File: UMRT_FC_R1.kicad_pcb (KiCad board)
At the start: 2 copper layers, 85 parts, among them J1 Conn_01x02, J10 Conn_01x04_Pin, J2 Conn_01x02_Pin, J3 Conn_01x02_Pin, J4 Conn_01x02_Pin, J5 Conn_01x02_Pin, J6 Conn_01x02_Pin, J7 Conn_01x04_Pin, J8 Conn_01x04_Pin, J9 Conn_01x04_Pin, U7 RP2040, U8 W25Q128JVS, Y1 Crystal_GND24

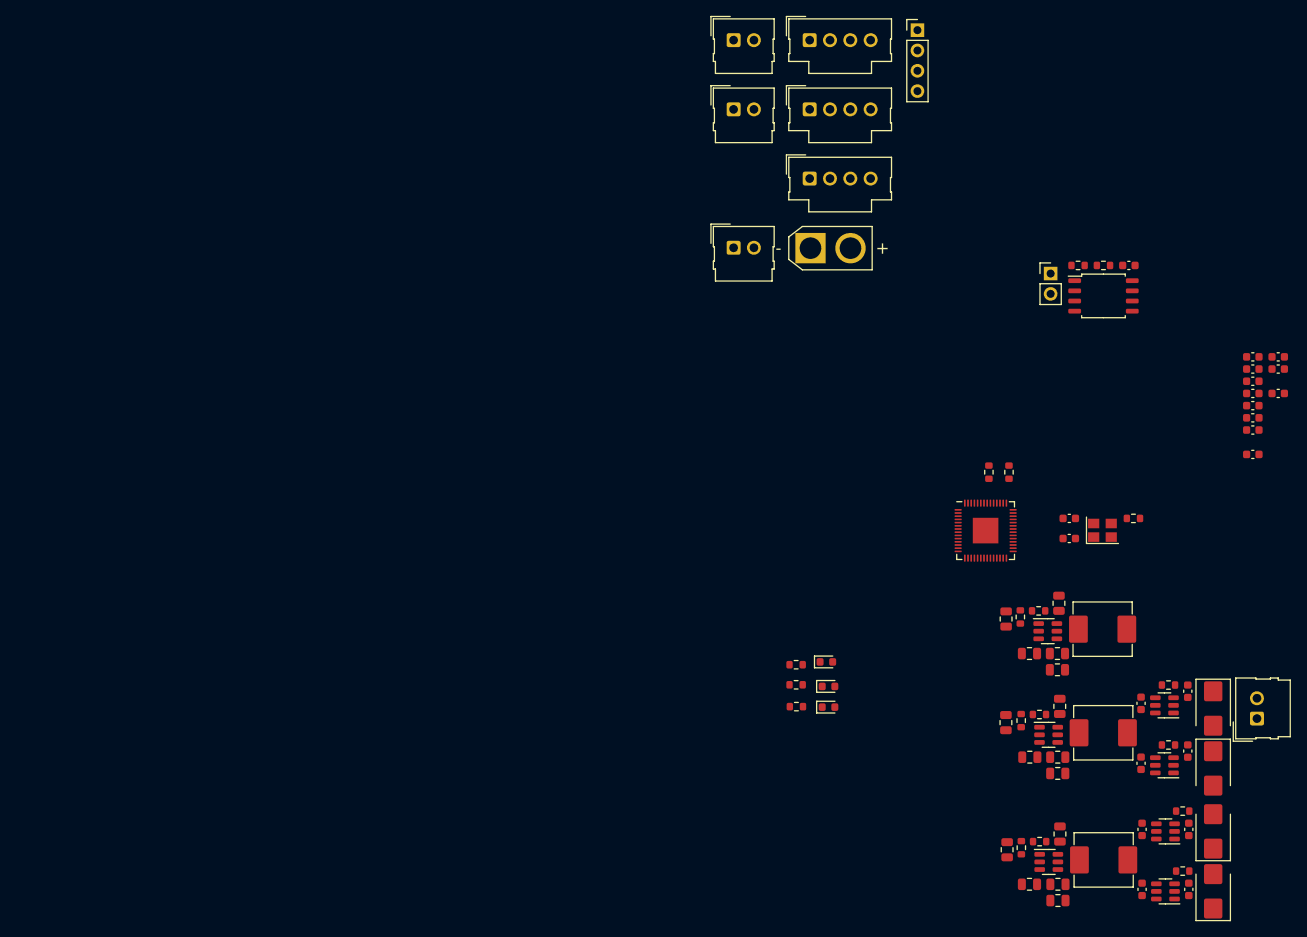
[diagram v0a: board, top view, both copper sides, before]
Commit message: started on layout and added SD/flash/BNO
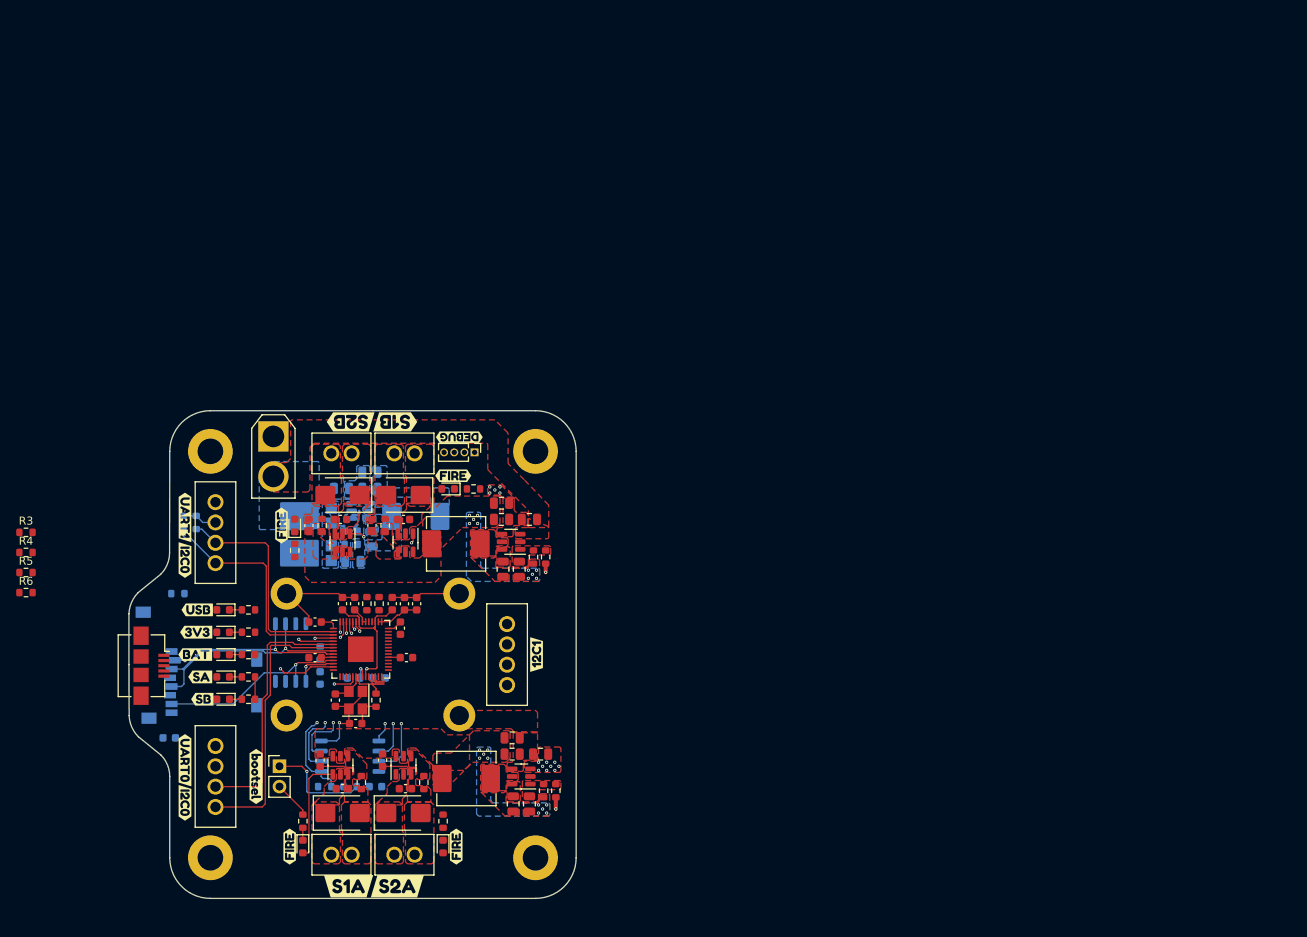
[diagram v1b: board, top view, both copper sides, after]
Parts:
- removed the R14 at (179.9, 120.8)
- removed the R16 at (179.9, 115.6)
- removed the R17 at (179.9, 118.1)
- added C38: 100n, Capacitor_SMD:C_0603_1608Metric, B.Cu at (101.5, 124.7)
- added C39: 100n, Capacitor_SMD:C_0603_1608Metric, B.Cu at (120.4, 117.2)
- added D10: LED, LED_SMD:LED_0603_1608Metric, F.Cu at (108.3, 117.1)
- added D11: LED, LED_SMD:LED_0603_1608Metric, F.Cu at (108.3, 119.9)
- added D12: LED, LED_SMD:LED_0603_1608Metric, F.Cu at (118.2, 138.3)
- added D13: LED, LED_SMD:LED_0603_1608Metric, F.Cu at (136.4, 93.6)
- added D14: LED, LED_SMD:LED_0603_1608Metric, F.Cu at (135.8, 138.3)
- added D15: LED, LED_SMD:LED_0603_1608Metric, F.Cu at (117.2, 98.2)
- added D6: MBR10, TO-227:TO-277-D, B.Cu at (120.7, 101.6)
- added D9: LED, LED_SMD:LED_0603_1608Metric, F.Cu at (108.3, 108.7)
- added G***: LOGO, Symbol:UMRT_16x16, B.Cu at (161.8, 114.3)
- added J1: USB_A, Connector_USB:USB_Micro-B_Amphenol_10104110_Horizontal, F.Cu at (99.3, 115.7)
- added J12: Micro_SD_Card, SD:CONN_3M_2900, B.Cu at (105.3, 115.7)
- added R1: 5k, Resistor_SMD:R_0603_1608Metric, B.Cu at (104.9, 97.8)
- added R2: 5k, Resistor_SMD:R_0603_1608Metric, B.Cu at (103.3, 97.8)
- added R22: 4.7k, Resistor_SMD:R_0603_1608Metric, B.Cu at (102.6, 106.7)
- added R23: 4.7k, Resistor_SMD:R_0603_1608Metric, B.Cu at (120.4, 114.1)
- added R24: 5k, Resistor_SMD:R_0603_1608Metric, F.Cu at (111.4, 114.3)
- added R25: 1k, Resistor_SMD:R_0603_1608Metric, F.Cu at (111.4, 111.5)
- added R26: 5k, Resistor_SMD:R_0603_1608Metric, F.Cu at (111.4, 108.7)
- added R27: 5k, Resistor_SMD:R_0603_1608Metric, F.Cu at (111.4, 117.1)
- added R28: 5k, Resistor_SMD:R_0603_1608Metric, F.Cu at (111.4, 119.9)
- added R29: 5k, Resistor_SMD:R_0603_1608Metric, F.Cu at (118.2, 135.1)
- added R3: 5k, Resistor_SMD:R_0603_1608Metric, F.Cu at (83.6, 99.0)
- added R30: 5k, Resistor_SMD:R_0603_1608Metric, F.Cu at (139.6, 93.6)
- added R31: 5k, Resistor_SMD:R_0603_1608Metric, F.Cu at (135.8, 135.1)
- added R32: 5k, Resistor_SMD:R_0603_1608Metric, F.Cu at (117.2, 101.3)
- added R4: 5k, Resistor_SMD:R_0603_1608Metric, F.Cu at (83.6, 101.5)
- added R5: 5k, Resistor_SMD:R_0603_1608Metric, F.Cu at (83.6, 104.0)
- added R6: 5k, Resistor_SMD:R_0603_1608Metric, F.Cu at (83.6, 106.6)
- added REF**: MountingHole_3.2mm_M3_DIN965_Pad, MountingHole:MountingHole_3.2mm_M3_DIN965_Pad, F.Cu at (147.3, 88.9)
- added REF**: MountingHole_3.2mm_M3_DIN965_Pad, MountingHole:MountingHole_3.2mm_M3_DIN965_Pad, F.Cu at (106.7, 88.9)
- added REF**: MountingHole_3.2mm_M3_DIN965_Pad, MountingHole:MountingHole_3.2mm_M3_DIN965_Pad, F.Cu at (147.3, 139.7)
- added REF**: MountingHole_3.2mm_M3_DIN965_Pad, MountingHole:MountingHole_3.2mm_M3_DIN965_Pad, F.Cu at (106.7, 139.7)
- added U1: ~, ada_bno055:adafruit_bno055_nopins, F.Cu at (127.0, 114.3)
- added U11: W25Q32JVSS, Package_SO:SOIC-8_5.23x5.23mm_P1.27mm, B.Cu at (116.7, 114.0)
- added kibuzzard-658B3C43: G***, kibuzzard-658B3C43, F.Cu at (129.8, 85.2)
- added kibuzzard-658B3C48: G***, kibuzzard-658B3C48, F.Cu at (124.2, 85.2)
- added kibuzzard-658B3F43: G***, kibuzzard-658B3F43, F.Cu at (103.5, 127.5)
- added kibuzzard-658B3F46: G***, kibuzzard-658B3F46, F.Cu at (103.5, 132.8)
- added kibuzzard-658B3F46: G***, kibuzzard-658B3F46, F.Cu at (103.5, 102.5)
- added kibuzzard-658B3FA3: G***, kibuzzard-658B3FA3, F.Cu at (103.5, 97.2)
- added kibuzzard-658B4089: G***, kibuzzard-658B4089, F.Cu at (112.4, 129.5)
- added kibuzzard-658C8ADE: G***, kibuzzard-658C8ADE, F.Cu at (105.0, 108.7)
- added kibuzzard-658C8AE5: G***, kibuzzard-658C8AE5, F.Cu at (104.9, 111.5)
- added kibuzzard-658C8AED: G***, kibuzzard-658C8AED, F.Cu at (104.8, 114.3)
- added kibuzzard-658C8AF6: G***, kibuzzard-658C8AF6, F.Cu at (105.4, 117.1)
- added kibuzzard-658C8AFA: G***, kibuzzard-658C8AFA, F.Cu at (105.7, 119.9)
- added kibuzzard-658C8B8E: G***, kibuzzard-658C8B8E, F.Cu at (137.4, 138.3)
- added kibuzzard-658C8B8E: G***, kibuzzard-658C8B8E, F.Cu at (116.6, 138.3)
- added kibuzzard-658C8B8E: G***, kibuzzard-658C8B8E, F.Cu at (115.6, 98.2)
- added kibuzzard-658C8B8E: G***, kibuzzard-658C8B8E, F.Cu at (137.0, 91.9)
- added kibuzzard-658C8C94: G***, kibuzzard-658C8C94, B.Cu at (104.6, 100.3)
- added kibuzzard-658C8C94: G***, kibuzzard-658C8C94, B.Cu at (104.3, 130.8)
- added kibuzzard-658C8C94: G***, kibuzzard-658C8C94, B.Cu at (141.0, 118.1)
- added kibuzzard-658C8CB0: G***, kibuzzard-658C8CB0, B.Cu at (104.6, 102.9)
- added kibuzzard-658C8CB0: G***, kibuzzard-658C8CB0, B.Cu at (104.3, 133.3)
- added kibuzzard-658C8CB0: G***, kibuzzard-658C8CB0, B.Cu at (141.0, 113.0)
- added kibuzzard-658C8CB5: G***, kibuzzard-658C8CB5, B.Cu at (140.8, 115.6)
- added kibuzzard-658C8CBA: G***, kibuzzard-658C8CBA, B.Cu at (141.0, 110.5)
- added kibuzzard-658C8CF0: G***, kibuzzard-658C8CF0, B.Cu at (110.0, 95.2)
- added kibuzzard-658C8CF0: G***, kibuzzard-658C8CF0, B.Cu at (110.0, 125.7)
- added kibuzzard-658C8CFC: G***, kibuzzard-658C8CFC, B.Cu at (110.1, 128.3)
- added kibuzzard-658C8CFC: G***, kibuzzard-658C8CFC, B.Cu at (110.5, 97.8)
- added kibuzzard-658C8D14: G***, kibuzzard-658C8D14, B.Cu at (110.5, 100.3)
- added kibuzzard-658C8D18: G***, kibuzzard-658C8D18, B.Cu at (110.5, 102.9)
- added kibuzzard-658C9743: G***, kibuzzard-658C9743, B.Cu at (110.2, 133.3)
- added kibuzzard-658C9748: G***, kibuzzard-658C9748, B.Cu at (110.2, 130.8)
- added kibuzzard-658C9778: G***, kibuzzard-658C9778, F.Cu at (130.0, 143.3)
- added kibuzzard-658C978A: G***, kibuzzard-658C978A, F.Cu at (124.0, 143.3)
- added kibuzzard-658C97C8: G***, kibuzzard-658C97C8, F.Cu at (147.4, 114.3)
- added kibuzzard-658CA21E: G***, kibuzzard-658CA21E, F.Cu at (137.8, 87.1)
- C21, C24, C32, C33, C34, C35, C36, C37, L3: moved to B.Cu
- D5: value LED -> MBR10; footprint LED_SMD:LED_0603_1608Metric -> TO-227:TO-277-D; moved to B.Cu
- J10: renamed from J9; footprint Connector_Molex:Molex_SL_171971-0004_1x04_P2.54mm_Vertical -> connector_molex_70543:molex_70543-0038_4pin
- J11: renamed from J10; footprint Connector_PinHeader_2.54mm:PinHeader_1x04_P2.54mm_Vertical -> Connector_PinHeader_1.27mm:PinHeader_1x04_P1.27mm_Vertical
- J4: renamed from J3; footprint Connector_Molex:Molex_SL_171971-0002_1x02_P2.54mm_Vertical -> connector_molex_70543:molex_70543-0036_2pin
- J5: renamed from J4; footprint Connector_Molex:Molex_SL_171971-0002_1x02_P2.54mm_Vertical -> connector_molex_70543:molex_70543-0036_2pin
- J6: renamed from J7; footprint Connector_Molex:Molex_SL_171971-0004_1x04_P2.54mm_Vertical -> connector_molex_70543:molex_70543-0038_4pin
- J7: renamed from J8; footprint Connector_Molex:Molex_SL_171971-0004_1x04_P2.54mm_Vertical -> connector_molex_70543:molex_70543-0038_4pin
- J8: renamed from J5; footprint Connector_Molex:Molex_SL_171971-0002_1x02_P2.54mm_Vertical -> connector_molex_70543:molex_70543-0036_2pin
- J9: renamed from J6; footprint Connector_Molex:Molex_SL_171971-0002_1x02_P2.54mm_Vertical -> connector_molex_70543:molex_70543-0036_2pin
- R18: renamed from R12; moved to B.Cu
- R19: renamed from R13; moved to B.Cu
- R20: renamed from R18; moved to B.Cu
- R21: renamed from R19; moved to B.Cu
- U10: renamed from U9; moved to B.Cu
- U9: renamed from U8; moved to B.Cu
- moved C31 121.0 mm to (119.8, 114.7), turned to 180 degrees
- moved C22 120.6 mm to (123.2, 107.9), turned to 90 degrees
- moved C25 119.7 mm to (119.8, 110.2), turned to 180 degrees
- moved C21 119.3 mm to (127.8, 117.2)
- moved J8 119.1 mm to (123.1, 89.2), turned to 180 degrees
- moved J6 118.3 mm to (107.3, 129.5), turned to -90 degrees
- moved C24 115.8 mm to (124.6, 117.2), turned to 180 degrees
- moved C28 115.7 mm to (124.7, 107.9), turned to 90 degrees
- moved C32 114.5 mm to (127.3, 130.8)
- moved R19 114.5 mm to (121.0, 130.8)
- moved R18 114.5 mm to (124.1, 130.8)
- moved J2 114.4 mm to (115.3, 128.3)
- moved C23 113.8 mm to (129.4, 107.9), turned to 90 degrees
- moved J4 113.0 mm to (123.1, 139.3)
- moved D4 112.1 mm to (123.2, 94.4), turned to 180 degrees
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- renumbered J1 to J2, J2 to J3, R4 to R10, R5 to R11, R6 to R12, R7 to R13, R8 to R14, R9 to R15, R10 to R16, R11 to R17, R1 to R7, R2 to R8, R3 to R9, U1 to U2, U2 to U3, U3 to U4, U4 to U5, U5 to U6, U6 to U7, U7 to U8
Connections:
- C33 pad 1: +24V -> Net-(D5-K)
- C9 pad 1: /IO/S2A_N -> /IO/S2A_P
- D1 pad 2: /IO/S1A_N -> GND
- D2 pad 1: /IO/S2A_N -> /IO/S2A_P
- D2 pad 2: /IO/S2A_P -> GND
- D3 pad 2: /IO/S1B_N -> GND
- D4 pad 2: /IO/S2B_N -> GND
- D5 pad 2: +3V3 -> +24V
- D8 pad 2: GND -> +3V3
- J10 pad 1: /IO/SCL/RX_B -> GND
- J10 pad 2: /IO/SDA/TX_B -> +3V3
- J10 pad 3: +3V3 -> /IO/SDA0/TX0
- J10 pad 4: GND -> /IO/SCL0/RX0
- J11 pad 1: /IO/SWDIO -> GND
- J11 pad 2: /IO/SWCLK -> +3V3
- J11 pad 3: +3V3 -> /IO/SWCLK
- J11 pad 4: GND -> /IO/SWDIO
- J3 pad 1: +24V -> GND
- J3 pad 2: GND -> +24V
- J4 pad 1: /IO/S1A_N -> /IO/S1A_P
- J4 pad 2: /IO/S1A_P -> GND
- J5 pad 1: /IO/S2A_N -> /IO/S2A_P
- J5 pad 2: /IO/S2A_P -> GND
- J6 pad 1: /IO/SCL/RX_A -> GND
- J6 pad 2: /IO/SDA/TX_A -> +3V3
- J6 pad 3: +3V3 -> /IO/SDA0/TX1
- J6 pad 4: GND -> /IO/SCL0/RX1
- J7 pad 1: /IO/SCL/RX_C -> GND
- J7 pad 2: /IO/SDA/TX_C -> +3V3
- J7 pad 3: +3V3 -> /IO/SDA1
- J7 pad 4: GND -> /IO/SCL1
- J8 pad 1: /IO/S2B_N -> /IO/S2B_P
- J8 pad 2: /IO/S2B_P -> GND
- J9 pad 1: /IO/S1B_N -> /IO/S1B_P
- J9 pad 2: /IO/S1B_P -> GND
- U10 pad 2: +24V -> Net-(D5-K)
- U10 pad 3: +24V -> Net-(D5-K)
- U4 pad 2: /IO/S2A_N -> /IO/S2A_P
- U8 pad 11: unconnected-(U7-GPIO8-Pad11) -> /RP2040/SPI_CIPO
- U8 pad 12: unconnected-(U7-GPIO9-Pad12) -> /RP2040/SPI_CS_FLASH
- U8 pad 13: unconnected-(U7-GPIO10-Pad13) -> /RP2040/SPI_CS_SD
- U8 pad 14: unconnected-(U7-GPIO11-Pad14) -> /RP2040/SPI_CS_EXTRA
- U8 pad 2: /IO/SDA/TX_A -> /IO/SDA0/TX0
- U8 pad 3: /IO/SCL/RX_A -> /IO/SCL0/RX0
- U8 pad 4: /IO/SCL/RX_C -> /IO/SDA1
- U8 pad 5: /IO/SDA/TX_C -> /IO/SCL1
- U8 pad 6: /IO/SDA/TX_B -> /IO/SDA0/TX1
- U8 pad 7: /IO/SCL/RX_B -> /IO/SCL0/RX1
- U8 pad 8: unconnected-(U7-GPIO6-Pad8) -> /RP2040/SPI_SCK
- U8 pad 9: unconnected-(U7-GPIO7-Pad9) -> /RP2040/SPI_COPI
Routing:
- net GND: track 0.00 -> 55.7 mm, vias 0 -> 9
- net /IO/SCL0/RX1: track 0.00 -> 34.4 mm
- net /IO/SDA0/TX1: track 0.00 -> 32.0 mm
- net /IO/SCL0/RX0: track 0.00 -> 29.5 mm
- net /IO/SDA0/TX0: track 0.00 -> 28.6 mm
- net /RP2040/SPI_SCK: track 0.00 -> 26.6 mm, vias 0 -> 1
- net /RP2040/QSPI_SS: track 0.00 -> 26.6 mm, vias 0 -> 2
- net /RP2040/SPI_COPI: track 0.00 -> 24.7 mm, vias 0 -> 1
- net /RP2040/SPI_CIPO: track 0.00 -> 24.5 mm, vias 0 -> 1
- net /RP2040/QSPI_SD3: track 0.00 -> 22.2 mm, vias 0 -> 2
- net +3V3: track 0.00 -> 21.4 mm, vias 0 -> 1
- net /RP2040/QSPI_SD1: track 0.00 -> 21.4 mm, vias 0 -> 2
- net /RP2040/QSPI_SD2: track 0.00 -> 20.8 mm, vias 0 -> 2
- net /RP2040/SPI_CS_SD: track 0.00 -> 20.8 mm, vias 0 -> 2
- net /RP2040/QSPI_SCLK: track 0.00 -> 19.7 mm, vias 0 -> 2
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- added copper zone on B.Cu, net +24V
- added copper zone on F.Cu, net +24V
- added copper zone on In1.Cu, net +24V
- added copper zone on B.Cu, net +3V3
- added copper zone on In1.Cu, net +3V3
- added copper zone on F.Cu, net /IO/S1A_P
- added copper zone on F.Cu, net /IO/S1B_P
- added copper zone on F.Cu, net /IO/S2A_P
- added copper zone on F.Cu, net /IO/S2B_P
- added copper zone on B.Cu, net /solenoid driver A/SPWR_A
- added copper zone on F.Cu, net /solenoid driver A/SPWR_A
- added copper zone on B.Cu, net /solenoid driver B/SPWR_B
- added copper zone on F.Cu, net /solenoid driver B/SPWR_B
- added copper zone on B.Cu, net GND
- added copper zone on F.Cu, net GND
- added copper zone on In2.Cu, net GND
- added copper zone on B.Cu, net Net-(D5-K)
- added copper zone on B.Cu, net Net-(U10-BST)
- added copper zone on B.Cu, net Net-(U10-FB)
- added copper zone on B.Cu, net Net-(U10-SW)
- added copper zone on F.Cu, net Net-(U2-ILIMIT)
- added copper zone on F.Cu, net Net-(U3-BST)
- added copper zone on F.Cu, net Net-(U3-FB)
- added copper zone on F.Cu, net Net-(U3-SW)
- added copper zone on F.Cu, net Net-(U4-ILIMIT)
- added copper zone on F.Cu, net Net-(U6-BST)
- added copper zone on F.Cu, net Net-(U6-FB)
- added copper zone on F.Cu, net Net-(U6-SW)
- added copper zone on F.Cu, net Net-(U7-ILIMIT)
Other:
- board outline added: 55.9 x 61 mm
- copper layers 2 -> 4
